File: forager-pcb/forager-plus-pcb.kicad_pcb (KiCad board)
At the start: 2 copper layers, 114.6 x 96.3 mm, 26 parts, among them J2 Conn_01x02_Pin, U1 XIAO nRF52840 Plus

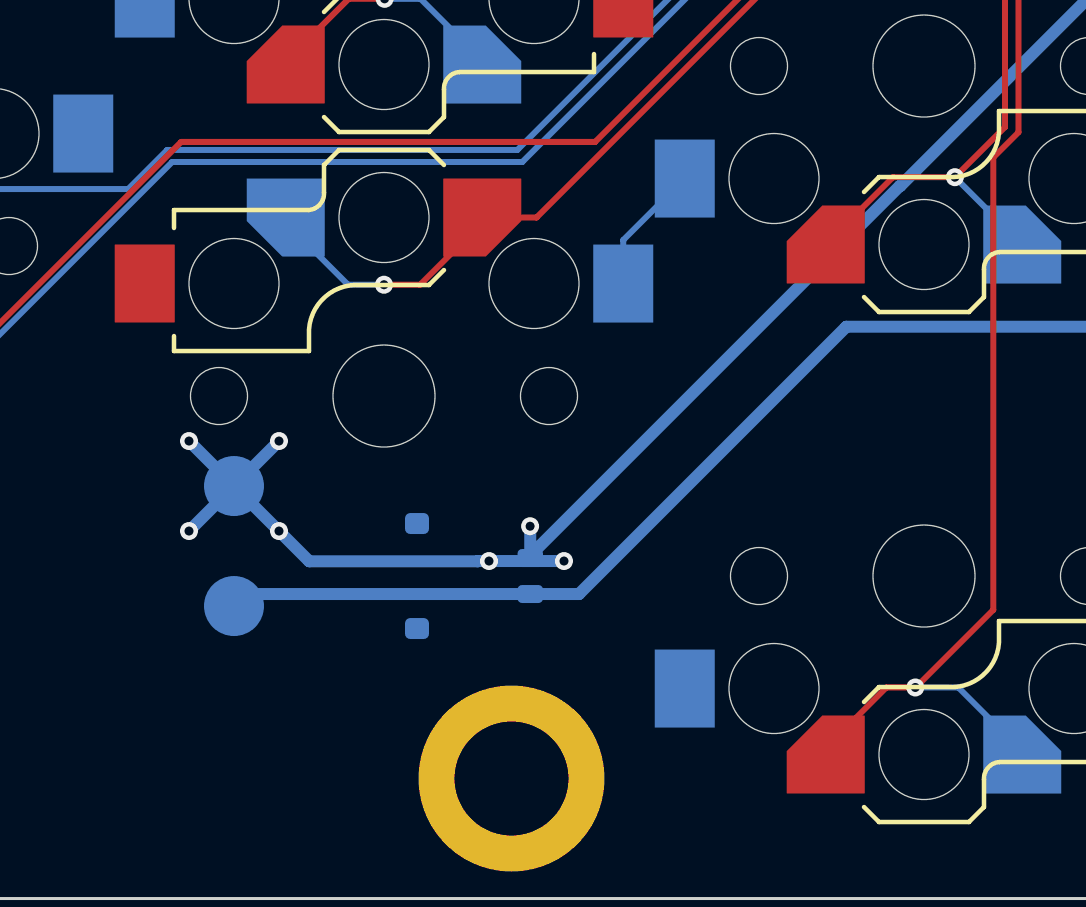
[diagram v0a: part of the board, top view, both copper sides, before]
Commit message: Use 2-pin horizontal SMD PicoBlade MX 1.25mm battery connector.
The inaccurate term JST 1.25mm, or 'Micro JST 1.25mm' is often
used for these. The connector socket is under 4mm so should fit,
and this is commonly offered as the connector with LiPo batteries.

Putting this on both sides in place of the original (harder to
find) connector and soldering points.
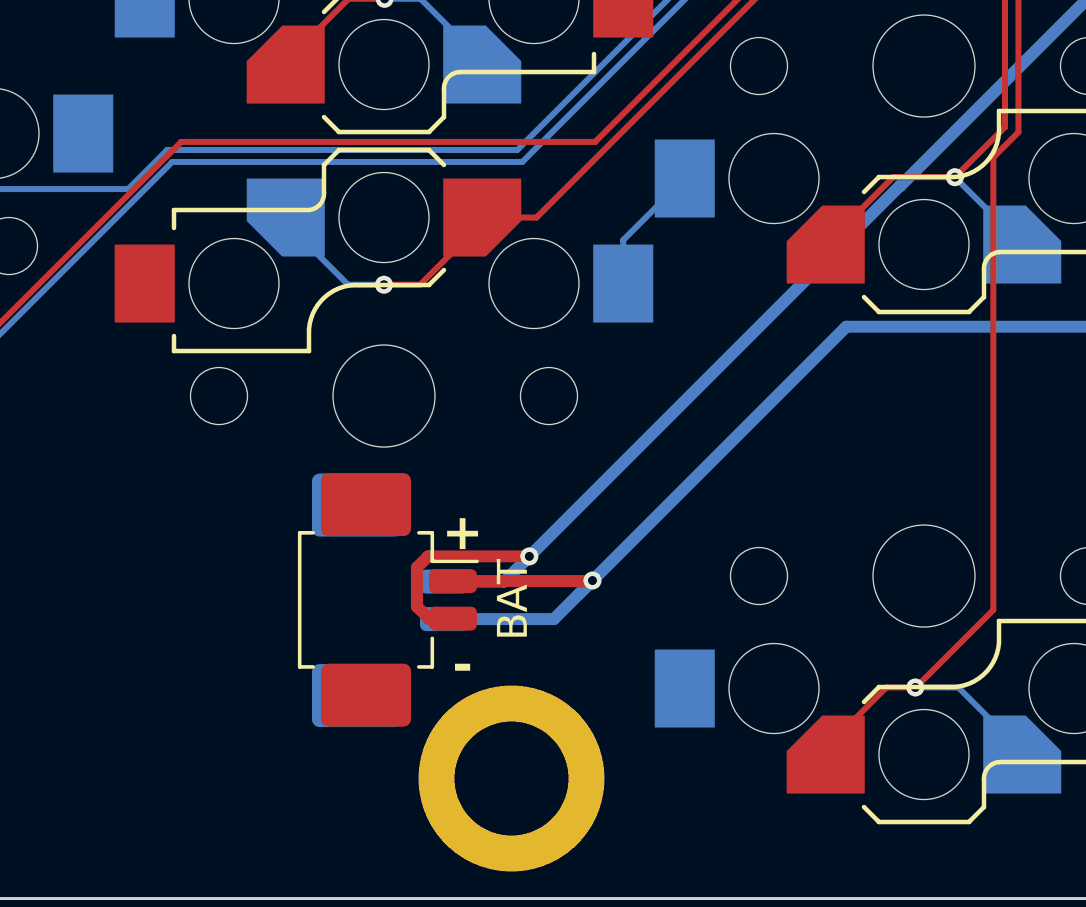
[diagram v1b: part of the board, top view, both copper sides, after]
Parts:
- removed J2: Conn_01x02_Pin, Connector_JST:JST_ACH_BM02B-ACHSS-GAN-ETF_1x02-1MP_P1.20mm_Vertical
- removed TP3, TP4: TestPoint, TestPoint:TestPoint_Pad_D2.0mm
- added BAT: Molex_PicoBlade_53261-0271_1x02-1MP_P1.25mm_Horizontal, Connector_Molex:Molex_PicoBlade_53261-0271_1x02-1MP_P1.25mm_Horizontal, F.Cu at (88.9, 6.79)
- added BAT: Molex_PicoBlade_53261-0271_1x02-1MP_P1.25mm_Horizontal, Connector_Molex:Molex_PicoBlade_53261-0271_1x02-1MP_P1.25mm_Horizontal, B.Cu at (88.6, 6.81)
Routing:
- net GND: track 122.2 -> 112.7 mm, vias 12 -> 6
- net BAT: track 88.1 -> 87.1 mm, vias 0 -> 1
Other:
- board text added: "-"

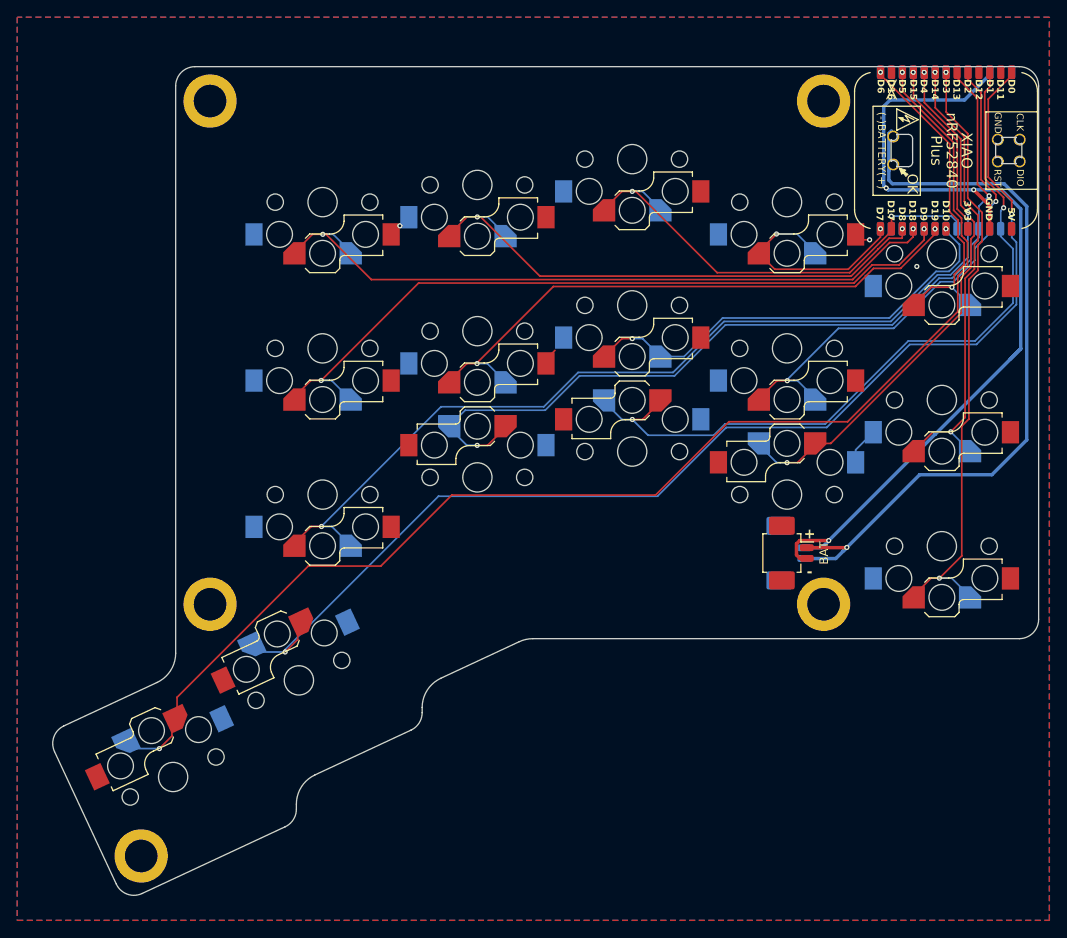
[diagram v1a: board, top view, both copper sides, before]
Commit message: Battery cutout by changing the PCB outline
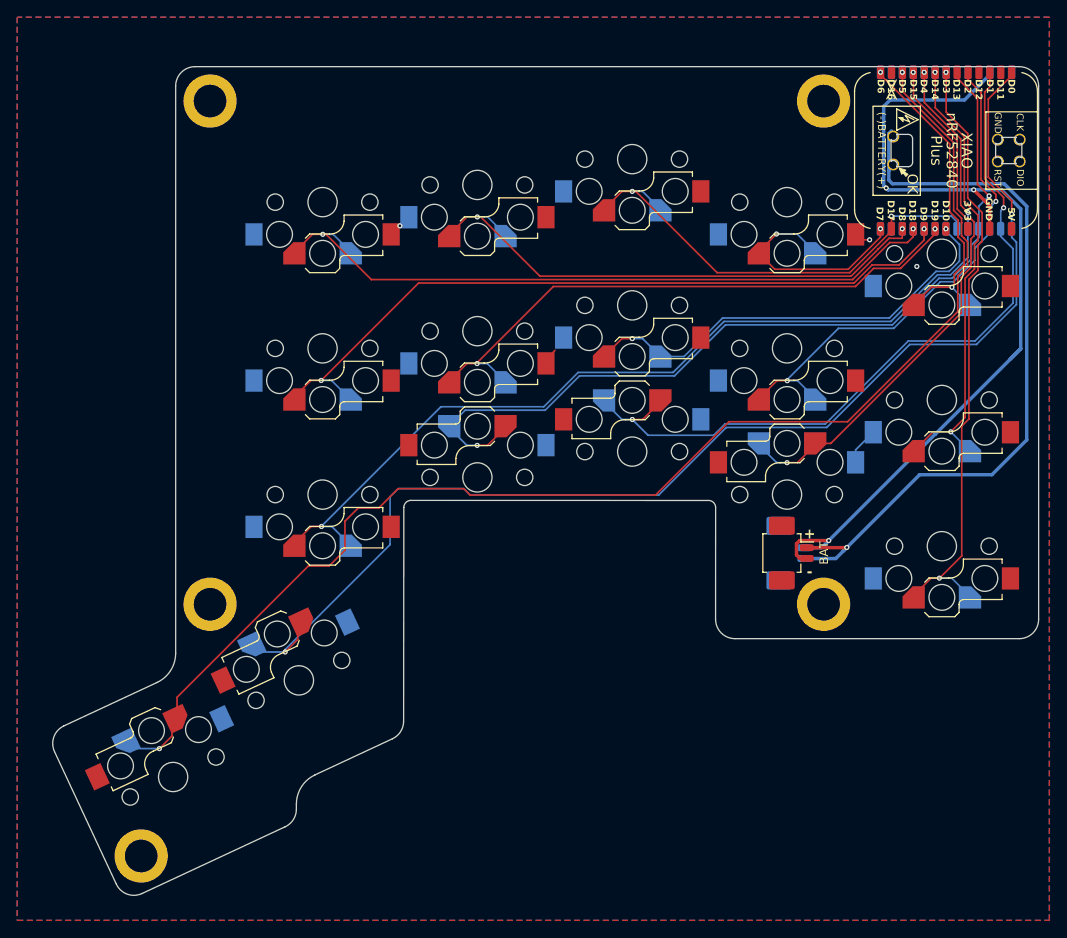
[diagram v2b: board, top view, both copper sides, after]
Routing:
- net RH1: track 137.7 -> 141.6 mm
- net RH0: track 149.8 -> 152.3 mm
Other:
- outline, holes or cut-outs redrawn

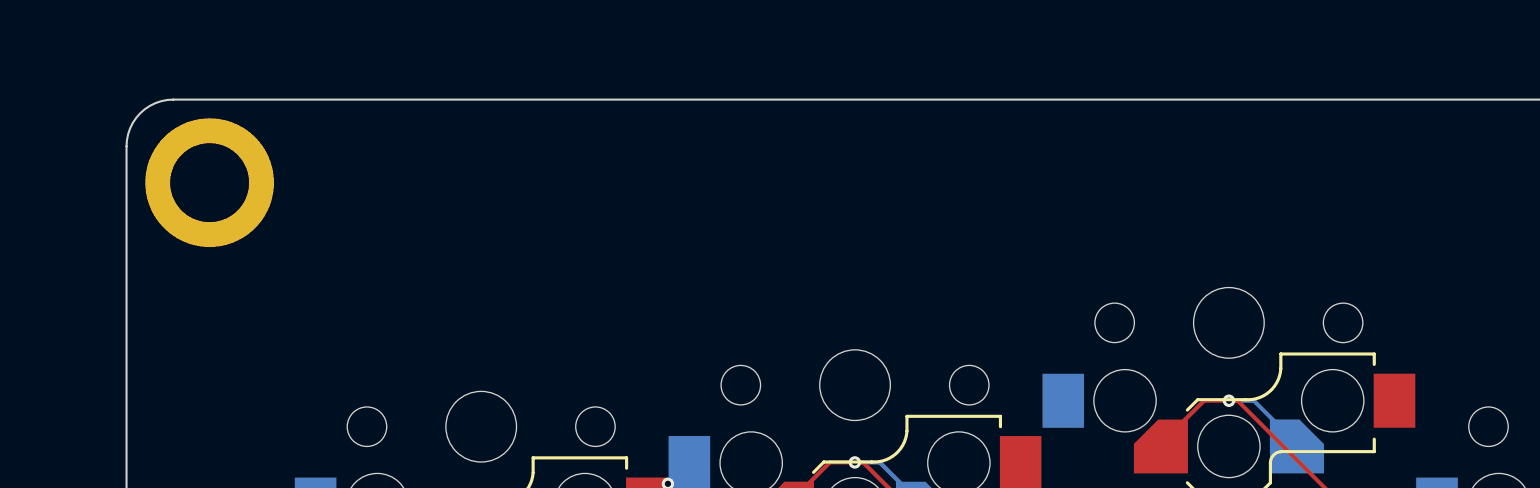
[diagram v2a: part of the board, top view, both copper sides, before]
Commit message: Adjust left/right labels and title on silkscreen
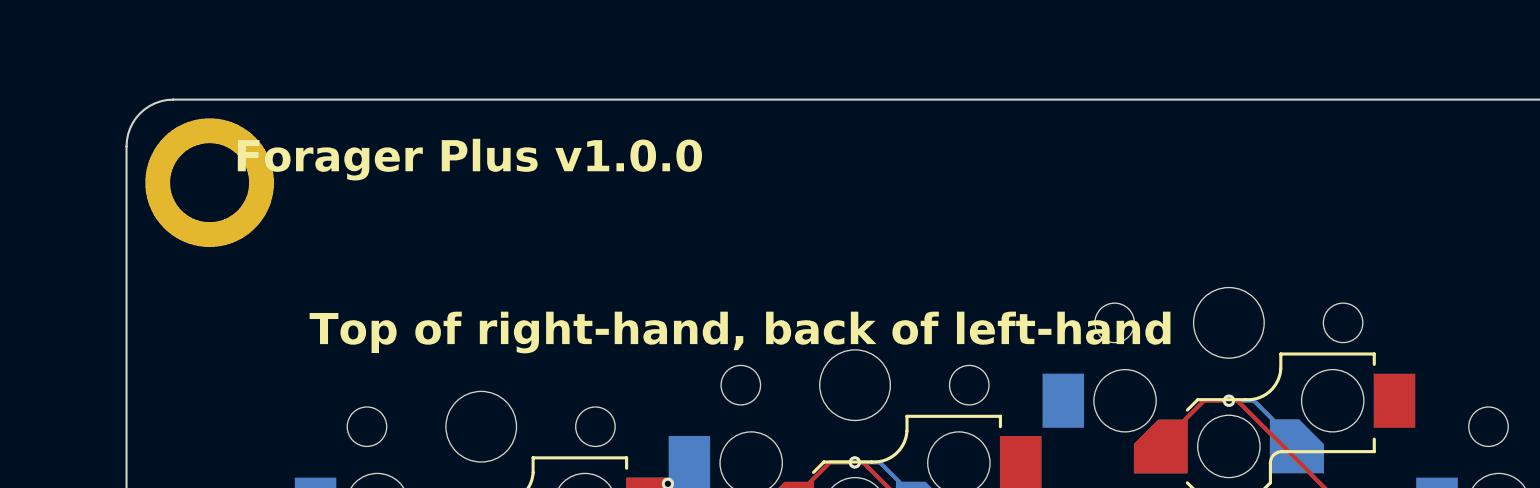
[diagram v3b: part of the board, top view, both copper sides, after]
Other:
- board text added: "Forager Plus v1.0.0"
- board text added: "Top of left-hand, back of right-hand"
- board text added: "Top of right-hand, back of left-hand"
- board text removed: "Back of right-hand"
- board text removed: "Forager Plus"
- board text removed: "Top of left-hand"

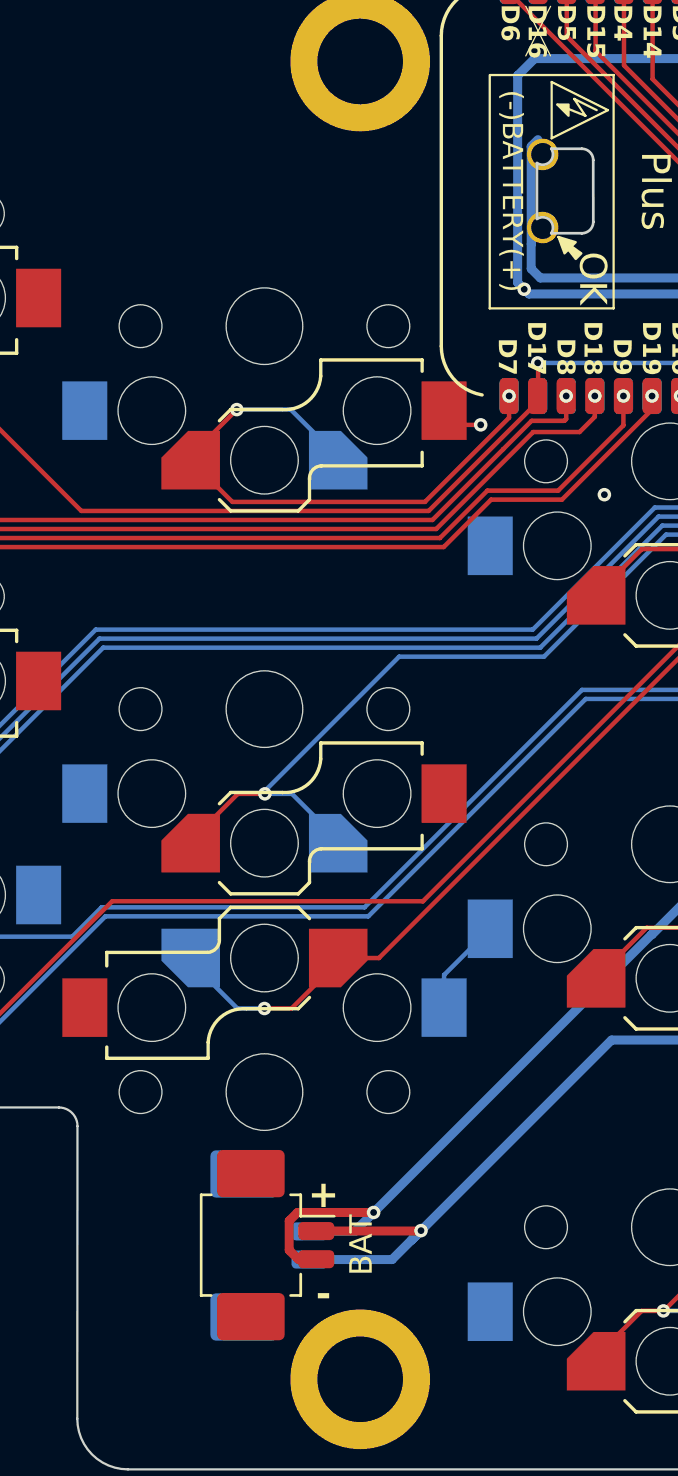
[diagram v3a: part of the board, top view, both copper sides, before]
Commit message: Move battery connector forward to avoid bottom case rib
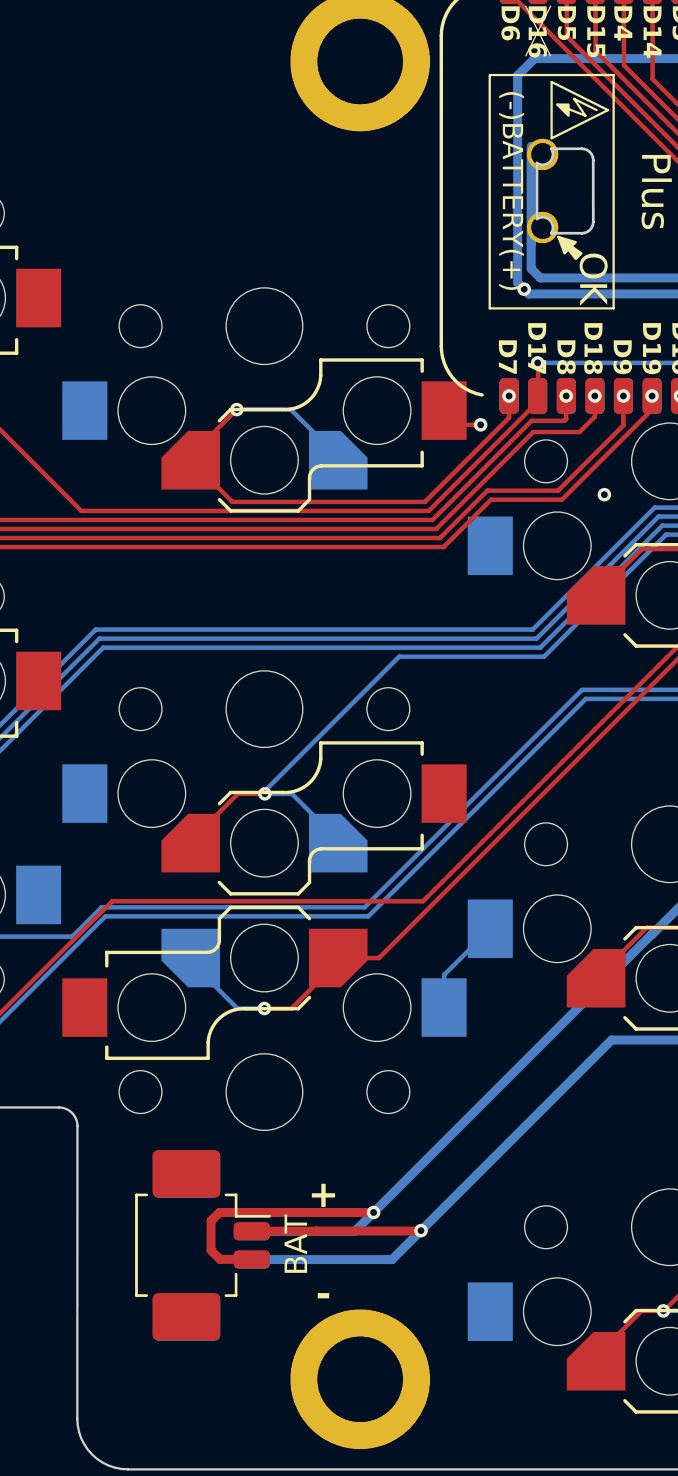
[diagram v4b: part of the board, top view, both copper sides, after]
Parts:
- moved BAT 2.87 mm to (86.0, 6.80)
- moved BAT 2.56 mm to (86.0, 6.81)
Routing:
- net GND: track 112.7 -> 118.4 mm
- net BAT: track 87.1 -> 92.7 mm
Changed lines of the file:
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@@
 	(footprint "Connector_Molex:Molex_PicoBlade_53261-0271_1x02-1MP_P1.25mm_Horizontal"
 		(layer "F.Cu")
-		(at 88.9 6.795 -90)
+		(at 86.03 6.8 -90)
 		(descr "Molex PicoBlade series connector, 53261-0271 (http://www.molex.com/pdm_docs/sd/532610271_sd.pdf), generated with kicad-footprint-generator")
 		(tags "connector Molex PicoBlade horizontal")
@@
 		(embedded_fonts no)
 		(model "${KICAD6}/8.0/3dmodels/PCM_marbastlib_custom/XIAO-nRF52840 v15.step"
+			(opacity 0.4200)
 			(offset
 				(xyz 6.1 -1.8 0.2)
@@
 			)
 		)
-		(model "/Users/peterjc/Downloads/xiao-nrf52840-sense-plus-v3.step"
+		(model "xiao-nrf52840-sense-plus-v3.step"
 			(offset
 				(xyz -6.1 -1.7 -1.6)
@@
 			)
 		)
-		(model "xiao-nrf52840-sense-plus-v3.step"
+		(model "/Users/peterjc/repositories/forager/case/Forager Case.step"
+			(opacity 0.4200)
 			(offset
-				(xyz -6.1 -1.7 -1.6)
+				(xyz 40 -107 -1.6)
 			)
 			(scale
@@
 			)
 			(rotate
-				(xyz 90 -0 -90)
+				(xyz -0 -0 -90)
 			)
 		)
@@
 	(footprint "Connector_Molex:Molex_PicoBlade_53261-0271_1x02-1MP_P1.25mm_Horizontal"
 		(layer "B.Cu")
-		(at 88.6 6.81 90)
+		(at 86.04 6.81 90)
 		(descr "Molex PicoBlade series connector, 53261-0271 (http://www.molex.com/pdm_docs/sd/532610271_sd.pdf), generated with kicad-footprint-generator")
 		(tags "connector Molex PicoBlade horizontal")
@@
 	)
 	(segment
-		(start 93.845434 5.345434)
-		(end 90.469082 5.345434)
+		(start 86.629 5.720516)
+		(end 86.629 7.024)
 		(width 0.4)
 		(layer "F.Cu")
@@
 	)
 	(segment
-		(start 110.7 -35.43)
-		(end 112.555 -33.575)
+		(start 86.629 7.024)
+		(end 87.03 7.425)
 		(width 0.4)
 		(layer "F.Cu")
@@
 	)
 	(segment
-		(start 62.02 -16.76)
-		(end 60.975 -15.715)
-		(width 0.2)
-		(layer "F.Cu")
-		(net 18)
-	)
-	(segment
-		(start 90.099 5.715516)
-		(end 90.099 7.019)
+		(start 87.004082 5.345434)
+		(end 86.629 5.720516)
 		(width 0.4)
 		(layer "F.Cu")
@@
 	)
 	(segment
-		(start 90.5 7.42)
-		(end 91.3 7.42)
+		(start 110.7 -35.43)
+		(end 112.555 -33.575)
 		(width 0.4)
 		(layer "F.Cu")
@@
 	)
 	(segment
-		(start 90.099 7.019)
-		(end 90.5 7.42)
-		(width 0.4)
+		(start 62.02 -16.76)
+		(end 60.975 -15.715)
+		(width 0.2)
 		(layer "F.Cu")
 		(net 18)
 	)
 	(segment
-		(start 90.469082 5.345434)
-		(end 90.099 5.715516)
+		(start 87.03 7.425)
+		(end 87.83 7.425)
 		(width 0.4)
 		(layer "F.Cu")
@@
 	)
 	(segment
-		(start 97.605 -29.62)
-		(end 96.975 -30.25)
-		(width 0.2)
+		(start 93.845434 5.345434)
+		(end 87.004082 5.345434)
+		(width 0.4)
 		(layer "F.Cu")
 		(net 18)
@@
 	)
 	(segment
-		(start 93.815434 5.375434)
-		(end 93.005868 6.185)
-		(width 0.4)
-		(layer "B.Cu")
-		(net 18)
-	)
-	(segment
-		(start 93.005868 6.185)
-		(end 91 6.185)
-		(width 0.4)
-		(layer "B.Cu")
-		(net 18)
-	)
-	(segment
 		(start 106.211 -7.001)
 		(end 116.17 -16.96)
@@
 	)
 	(segment
+		(start 93.815434 5.375434)
+		(end 93.005868 6.185)
+		(width 0.4)
+		(layer "B.Cu")
+		(net 18)
+	)
+	(segment
 		(start 100.74 -35.43)
 		(end 110.7 -35.43)
@@
 	)
 	(segment
+		(start 93.005868 6.185)
+		(end 87.84 6.185)
+		(width 0.4)
+		(layer "B.Cu")
+		(net 18)
+	)
+	(segment
 		(start 114.91 -15.7)
 		(end 116.17 -16.96)
@@
 	)
 	(segment
+		(start 91.3 6.17)
+		(end 91.295 6.175)
+		(width 0.4)
+		(layer "F.Cu")
+		(net 19)
+	)
+	(segment
 		(start 95.93 6.17)
 		(end 91.3 6.17)
@@
 		(net 19)
 	)
+	(segment
+		(start 91.295 6.175)
+		(end 87.83 6.175)
+		(width 0.4)
+		(layer "F.Cu")
+		(net 19)
+	)
 	(via
 		(at 95.95 6.15)
@@
 	)
 	(segment
-		(start 95.5 6.6)
-		(end 95.88 6.22)
-		(width 0.4)
-		(layer "B.Cu")
-		(net 19)
-	)
-	(segment
 		(start 94.665 7.435)
-		(end 91 7.435)
+		(end 87.84 7.435)
 		(width 0.4)
 		(layer "B.Cu")
@@
 	)
 	(segment
-		(start 101.249 -36.141)
-		(end 100.841 -36.549)
+		(start 94.665 7.435)
+		(end 95.95 6.15)
 		(width 0.4)
 		(layer "B.Cu")
@@
 	)
 	(segment
-		(start 95.88 6.22)
-		(end 94.665 7.435)
+		(start 101.249 -36.141)
+		(end 100.841 -36.549)
 		(width 0.4)
 		(layer "B.Cu")
@@
 	)
 	(segment
-		(start 100.841 -41.981)
-		(end 101.14 -42.28)
-		(width 0.4)
-		(layer "B.Cu")
-		(net 19)
-	)
-	(segment
 		(start 95.95 6.15)
 		(end 104.41 -2.31)
@@
 		(width 0.4)
 		(layer "B.Cu")
-		(net 19)
-	)
-	(segment
-		(start 95.88 6.22)
-		(end 95.95 6.15)
-		(width 0.4)
-		(layer "B.Cu")
